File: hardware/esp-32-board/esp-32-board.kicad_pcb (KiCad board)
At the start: 2 copper layers, 53.4 x 68.6 mm, 36 parts, among them J1 ESP-PROG-Program, J2 MainConnector, J3 ESP-PROG-Debug, J4 Conn_01x06, J5 Barrel_Jack_MountingPin, J7 USB_B_Micro, Q1 BCR129S, SW1 SW_Push, SW2 SW_Push, U1 ESP32-WROOM-32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

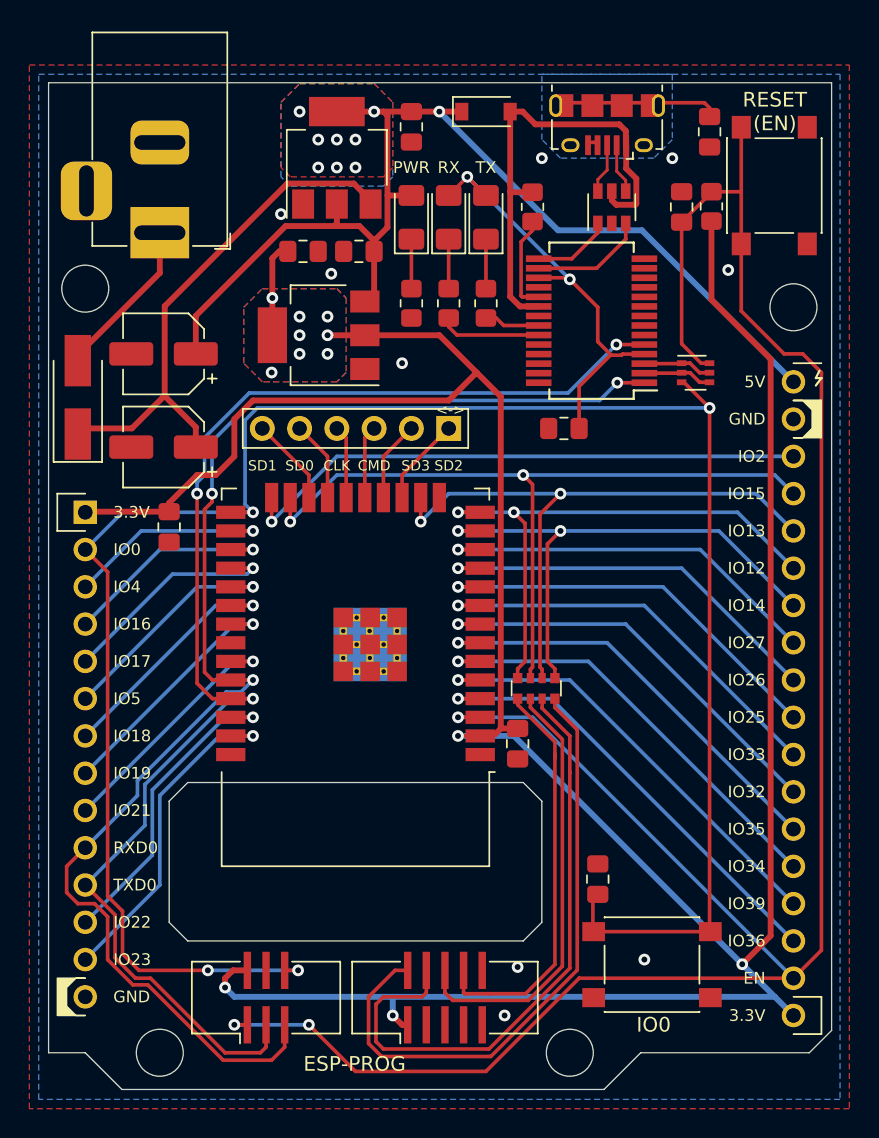
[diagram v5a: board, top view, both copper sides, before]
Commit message: Add pullup for IO0
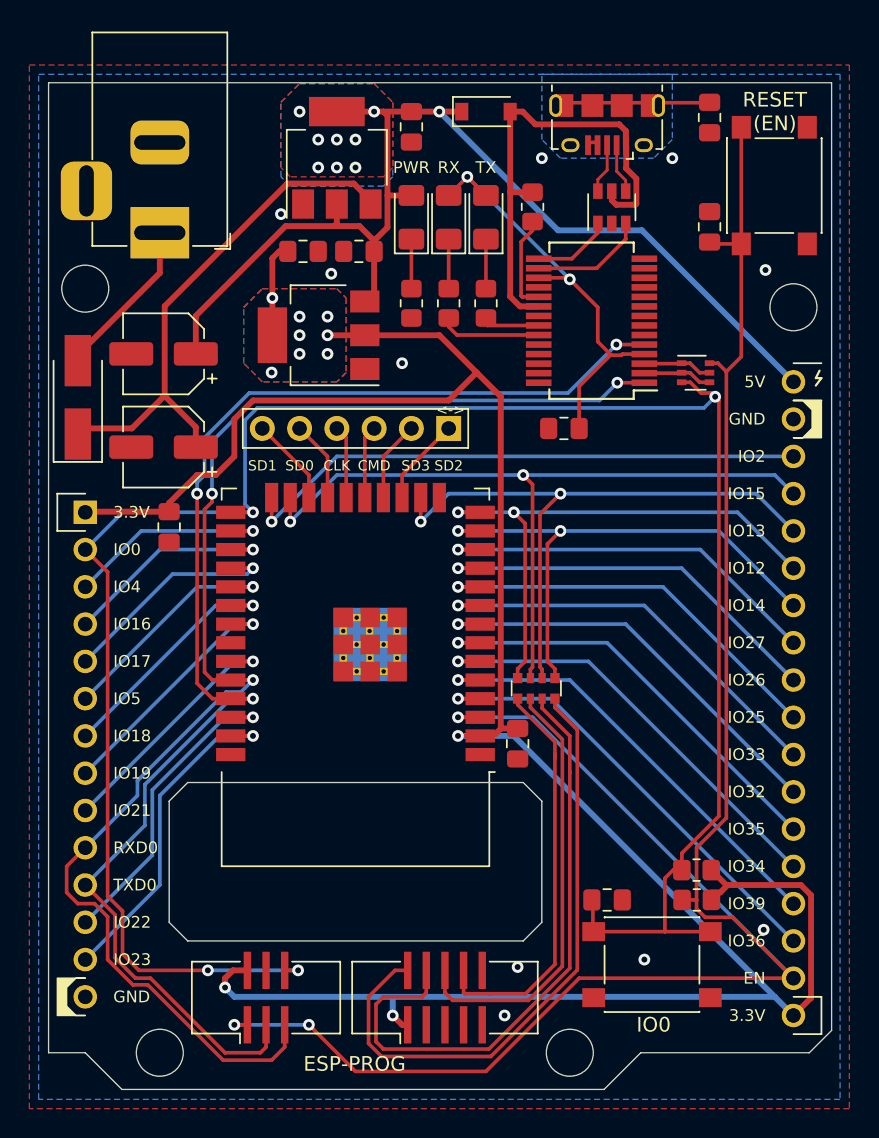
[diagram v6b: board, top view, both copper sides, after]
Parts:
- added R6: 10k Ohm, Resistor_SMD:R_0805_2012Metric_Pad1.20x1.40mm_HandSolder, F.Cu at (173.7, 75.2)
- moved R5 47.3 mm to (173.8, 77.2), turned to 180 degrees
- moved C3 2.34 mm to (174.6, 31.3)
- moved C2 1.55 mm to (167.6, 77.2), turned to 180 degrees
- moved C10 0.97 mm to (174.6, 23.9)
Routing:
- net +3V3: track 205.9 -> 170.3 mm, vias 12 -> 11
- net /EN: track 152.1 -> 142.6 mm
- net /IO0: track 143.4 -> 147.1 mm
- net Net-(C10-Pad1): track 10.6 -> 9.53 mm
- net GND: vias 9 -> 10

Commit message: Move C11 and U3
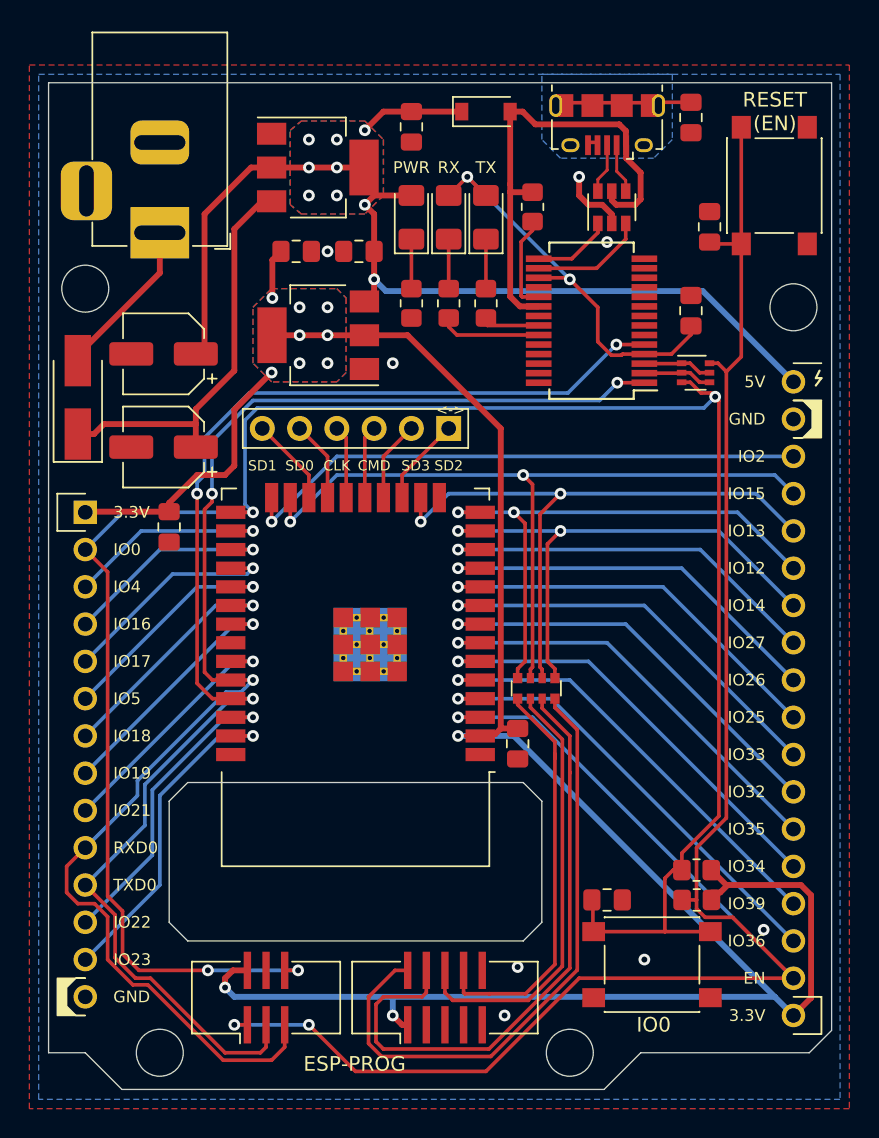
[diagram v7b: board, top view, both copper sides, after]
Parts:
- moved C11 11.8 mm to (173.4, 37.1), turned to 90 degrees
- moved U3 1.45 mm to (147.9, 27.3), turned to 0 degrees
- moved C10 1.27 mm to (173.4, 23.9)
- moved C6 0.47 mm to (146.5, 33.0)
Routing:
- net +3V3: track 170.3 -> 156.5 mm
- net VDC: track 35.7 -> 27.7 mm
- net GND: track 1.46 -> 6.11 mm, vias 10 -> 8
- net +5V: track 75.3 -> 73.3 mm
- net Net-(C10-Pad1): track 9.53 -> 8.11 mm
- net /USB/USB_3V3: track 29.6 -> 28.6 mm

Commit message: CI: fix errors (#2)
* CI: fix errors

* Cosmetic fixes on PCB

* Change build trigger conditions

* Regenerate cooper zones

* Cosmetic fixes on PCB

* Mark ESP-PROG as SMD
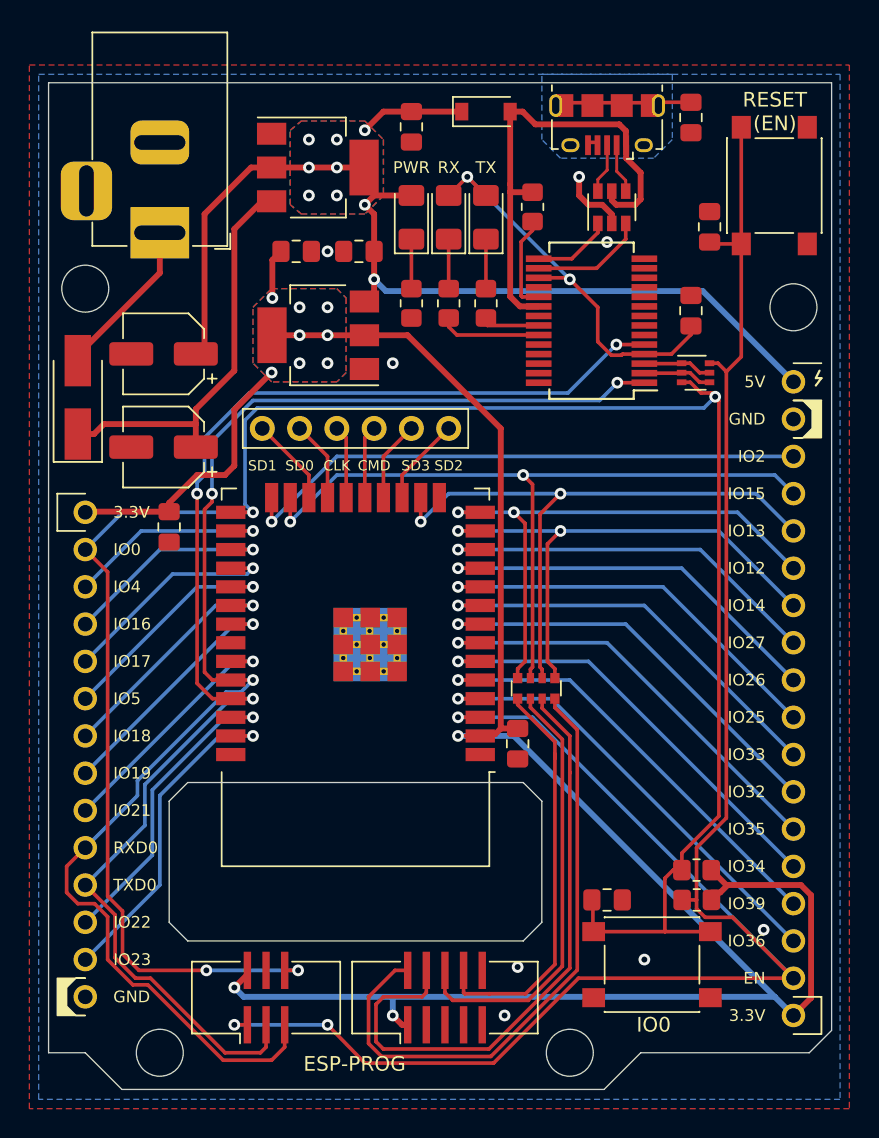
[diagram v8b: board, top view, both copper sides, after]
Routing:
- net +3V3: track 156.5 -> 156.0 mm
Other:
- board text removed: "<->"
